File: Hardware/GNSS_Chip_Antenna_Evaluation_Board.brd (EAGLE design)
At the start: 61 x 35.6 mm, 70 parts, among them J1 U.FL, J2 U.FL, J3 U.FL, J4 U.FL, J5 U.FL, J6 U.FL, Y2 PUCK, Y3 CUBE, Y4 CHIP, Y5 MOLDED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

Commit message: Removing lib. Adding test result images.
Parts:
- R1: device Testing:0402-RES -> SparkFun-Resistors:0402
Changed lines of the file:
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@@
 <?xml version="1.0" encoding="utf-8"?>
 <!DOCTYPE eagle SYSTEM "eagle.dtd">
-<eagle version="9.2.2">
+<eagle version="9.3.0">
 <drawing>
 <settings>
@@
 </element>
 <element name="Y4" library="GNSS_Chip_Antenna_Evaluation_Board" package="MOLEX_GNSS_CHIP" value="CHIP" x="52.07" y="1.143" smashed="yes"/>
-<element name="R1" library="Testing" package="0402-RES" value="0" x="56.007" y="1.651" smashed="yes" rot="R180">
+<element name="R1" library="SparkFun-Resistors" package="0402" value="0" x="56.007" y="1.651" smashed="yes" rot="R180">
 <attribute name="NAME" x="56.896" y="0.9525" size="0.4064" layer="25" rot="R180"/>
-<attribute name="VALUE" x="57.0865" y="2.794" size="0.4064" layer="27" rot="R180"/>
+<attribute name="PROD_ID" value="RES-14244" x="56.007" y="1.651" size="1.778" layer="27" rot="R180" display="off"/>
+<attribute name="VALUE" value="0" x="57.0865" y="2.794" size="0.4064" layer="27" rot="R180"/>
 </element>
 <element name="J4" library="SparkFun-Connectors" package="U.FL" value="U.FL" x="57.716" y="3.81" smashed="yes" rot="R270">
@@
 <contactref element="R1" pad="1"/>
 <contactref element="J4" pad="FEED"/>
-<wire x1="56.657" y1="1.651" x2="57.382" y2="1.651" width="0.878840625" layer="1"/>
+<wire x1="56.587" y1="1.651" x2="57.382" y2="1.651" width="0.878840625" layer="1"/>
 <wire x1="57.716" y1="1.985" x2="57.716" y2="2.285" width="0.878840625" layer="1"/>
 <wire x1="57.716" y1="1.985" x2="57.382" y2="1.651" width="0.878840625" layer="1"/>
@@
 <contactref element="Y4" pad="FEED"/>
 <wire x1="54.453" y1="1.693" x2="53.52" y2="1.693" width="0.4826" layer="1"/>
-<wire x1="55.357" y1="1.651" x2="54.483" y2="1.651" width="0.878840625" layer="1"/>
+<wire x1="55.427" y1="1.651" x2="54.483" y2="1.651" width="0.878840625" layer="1"/>
 <wire x1="54.483" y1="1.651" x2="54.483" y2="1.663" width="0.2032" layer="1"/>
 <wire x1="54.483" y1="1.663" x2="54.453" y2="1.693" width="0.2032" layer="1"/>

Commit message: Pass review: Change silk. Add dims. Revise a few FPs.
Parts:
- removed U$40: (no value), buzzard_labels (14):MOLEX_CUBE6
- removed U$41: (no value), buzzard_labels (14):TE_PUCK5
- removed U$45: (no value), buzzard_labels (61):W3062A1
- added U$43: (no value), buzzard_labels (1):ANTENNA10
- added U$50: (no value), buzzard_labels (1):EVALUATION_BOARD15
- added U$52: (no value), buzzard_labels (1):GNSS_CHIP13
- added U$56: (no value), buzzard_labels (1):MOLEX_CUBE6
- added U$57: (no value), buzzard_labels (1):TE_PUCK7
- added U$58: (no value), buzzard_labels (1):W3062A3
- added U$59: (no value), buzzard_labels (1):W30112
- U$13: device buzzard_labels (13):W30111 -> buzzard_labels (1):TE_PUCK7
- U$19: device buzzard_labels (14):MOLEX_CHIP7 -> buzzard_labels (1):MOLEX_CHIP5
- U$20: device buzzard_labels (14):MOLEX_CUBE6 -> buzzard_labels (1):MOLEX_CHIP5
- U$21: device buzzard_labels (60):MOLEX1 -> buzzard_labels (1):MOLEX0
- U$22: device buzzard_labels (14):TE_PUCK5 -> buzzard_labels (1):MOLEX0
- U$29: device buzzard_labels (60):MOLDED2 -> buzzard_labels (1):MOLDED1
- U$30: device buzzard_labels (60):MOLEX1 -> buzzard_labels (1):MOLDED1
- U$31: device buzzard_labels (60):MOLDED2 -> buzzard_labels (1):MOLEX_CUBE6
- U$33: device buzzard_labels (13):W30111 -> buzzard_labels (1):W30112
- U$35: device buzzard_labels (14):W3062A9 -> buzzard_labels (1):W3062A3
- U$37: device buzzard_labels (14):MOLEX_CHIP7 -> SparkFun-Aesthetics:SFE_LOGO_NAME_FLAME_.1
- Y2: device GNSS_Chip_Antenna_Evaluation_Board:TE_PUCK -> SparkFun-GPS:TE_PUCK
- Y3: device GNSS_Chip_Antenna_Evaluation_Board:MOLEX_GNSS_CUBE -> SparkFun-GPS:MOLEX_GNSS_CUBE
- Y4: device GNSS_Chip_Antenna_Evaluation_Board:MOLEX_GNSS_CHIP -> SparkFun-GPS:MOLEX_GNSS_CHIP
- Y5: device GNSS_Chip_Antenna_Evaluation_Board:MLOEX_GNSS_MOLDED -> SparkFun-GPS:MLOEX_GNSS_MOLDED
- Y6: device GNSS_Chip_Antenna_Evaluation_Board:W3062A -> SparkFun-GPS:W3062A
- Y7: device GNSS_Chip_Antenna_Evaluation_Board:W3011 -> SparkFun-GPS:W3011
- moved U$37 48.3 mm to (12.8, 9.65)
- moved U$20 29.7 mm to (60.5, 16.9), flipped to the bottom
- moved U$31 27.5 mm to (43.1, 12.7)
- moved U$22 27.4 mm to (13.1, 31.8), turned to 0 degrees
- moved U$13 23.1 mm to (25.8, 7.24), flipped to the bottom
- moved U$16 17.8 mm to (36.8, 2.54)
- moved U$42 9.72 mm to (24.1, 5.33)
- moved U$30 8.66 mm to (21.5, 29.5), flipped to the bottom
- moved U$35 1.78 mm to (53.8, 35.8)
- moved U$29 0.25 mm to (12.3, 29.5)
- moved U$33 0.18 mm to (44.5, 27.4)
- moved U$21 0.13 mm to (20.7, 31.8)
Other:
- board text added: "Units in inches"

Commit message: Add schematic title. Bump fiducials. Move version #.
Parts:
- moved FRAME1 3.59 mm to (3.81, -12.7)
- moved JP8 0.13 mm to (49.0, 34.8)
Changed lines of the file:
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@@
 <layer number="44" name="Drills" color="7" fill="1" visible="no" active="yes"/>
 <layer number="45" name="Holes" color="7" fill="1" visible="yes" active="yes"/>
-<layer number="46" name="Milling" color="3" fill="1" visible="yes" active="yes"/>
-<layer number="47" name="Measures" color="7" fill="1" visible="yes" active="yes"/>
+<layer number="46" name="Milling" color="3" fill="1" visible="no" active="yes"/>
+<layer number="47" name="Measures" color="7" fill="1" visible="no" active="yes"/>
 <layer number="48" name="Document" color="7" fill="1" visible="no" active="yes"/>
 <layer number="49" name="ReferenceLC" color="13" fill="1" visible="no" active="yes"/>
@@
 <wire x1="0" y1="0" x2="0" y2="35.56" width="0.2032" layer="20"/>
 <text x="0" y="-0.0635" size="0.0254" layer="214" font="vector">D:/SmartProjects/Snc/a4_bn_logo2.bmp</text>
-<text x="20.701" y="0.254" size="1.27" layer="16" font="vector" ratio="20" rot="MR0">V10</text>
+<text x="19.304" y="0.889" size="1.27" layer="16" font="vector" ratio="20" rot="MR0" align="center">V10</text>
 <wire x1="25.4" y1="35.56" x2="25.4" y2="0" width="0.2032" layer="20"/>
 <text x="67.31" y="39.37" size="1.27" layer="51">0.8mm Board Thickness</text>
@@
 <element name="JP5" library="SparkFun" package="STAND-OFF" value="STAND-OFF" x="45.72" y="20.32" smashed="yes" rot="R180"/>
 <element name="JP6" library="SparkFun" package="STAND-OFF" value="STAND-OFF" x="27.94" y="33.02" smashed="yes" rot="R180"/>
-<element name="JP8" library="SparkFun" package="FIDUCIAL-1X2" value="FIDUCIAL1X2" x="49.022" y="34.671" smashed="yes"/>
+<element name="JP8" library="SparkFun" package="FIDUCIAL-1X2" value="FIDUCIAL1X2" x="49.022" y="34.798" smashed="yes"/>
 <element name="JP9" library="SparkFun" package="FIDUCIAL-1X2" value="FIDUCIAL1X2" x="0.762" y="0.762" smashed="yes"/>
 <element name="U$16" library="SparkFun-Aesthetics" package="OSHW-LOGO-S" value="OSHW-LOGOS" x="36.83" y="2.54" smashed="yes" rot="MR0"/>
-<element name="FRAME1" library="SparkFun-Aesthetics" package="CREATIVE_COMMONS" value="FRAME-LETTER" x="1.27" y="-15.24" smashed="yes">
-<attribute name="DESIGNER" value="" x="1.27" y="-15.24" size="1.778" layer="27" font="vector" ratio="15" display="off"/>
-<attribute name="REV" value="" x="1.27" y="-15.24" size="1.778" layer="27" font="vector" ratio="15" display="off"/>
-</element>
 <element name="J1" library="SparkFun-Connectors" package="U.FL" value="U.FL" x="34.29" y="32.004" smashed="yes" rot="R90">
 <attribute name="NAME" x="31.75" y="30.734" size="0.6096" layer="25" font="vector" ratio="20" rot="R90"/>
@@
 <element name="U$35" library="buzzard_labels (1)" package="W3062A3" value="" x="53.848" y="35.814" smashed="yes" rot="MR270"/>
 <element name="U$37" library="SparkFun-Aesthetics" package="SFE_LOGO_NAME_FLAME_.1" value="" x="12.827" y="9.652" smashed="yes" rot="MR0"/>
+<element name="FRAME1" library="SparkFun-Aesthetics" package="CREATIVE_COMMONS" value="FRAME-LETTER" x="3.81" y="-12.7" smashed="yes">
+<attribute name="DESIGNER" value="" x="3.81" y="-12.7" size="1.778" layer="27" font="vector" ratio="15" display="off"/>
+<attribute name="REV" value="" x="3.81" y="-12.7" size="1.778" layer="27" font="vector" ratio="15" display="off"/>
+</element>
 </elements>
 <signals>
@@
 <contactref element="Y7" pad="1"/>
 <wire x1="38.7934" y1="33.815" x2="39.04" y2="33.815" width="0.1524" layer="1"/>
-<wire x1="38.387" y1="33.815" x2="39.04" y2="33.815" width="0.2032" layer="1"/>
 <wire x1="34.29" y1="33.529" x2="34.576" y2="33.815" width="0.878840625" layer="1"/>
-<wire x1="34.576" y1="33.815" x2="38.387" y2="33.815" width="0.878840625" layer="1"/>
+<wire x1="38.387" y1="33.815" x2="34.576" y2="33.815" width="0.878840625" layer="1"/>
+<wire x1="39.04" y1="33.815" x2="38.387" y2="33.815" width="0.1524" layer="1"/>
 </signal>
 <signal name="FEED3">
@@
 <contactref element="J3" pad="FEED"/>
 <contactref element="Y3" pad="FEED"/>
-<wire x1="31.36158125" y1="9.779" x2="31.39058125" y2="9.75" width="0.878840625" layer="1"/>
 <wire x1="29.465" y1="9.779" x2="31.36158125" y2="9.779" width="0.878840625" layer="1"/>
 <wire x1="31.5" y1="9.75" x2="31.471" y2="9.779" width="0.2032" layer="1"/>
@@
 <contactref element="J5" pad="FEED"/>
 <wire x1="2.159" y1="29.211003125" x2="2.159" y2="32.004996875" width="0.878840625" layer="1"/>
-<wire x1="2.159" y1="32.004996875" x2="2.114" y2="32.049996875" width="0.878840625" layer="1"/>
 <wire x1="2.114" y1="32.05" x2="2.159" y2="32.005" width="0.2032" layer="1"/>
 <wire x1="2.159" y1="32.005" x2="2.159" y2="32.004996875" width="0.2032" layer="1"/>

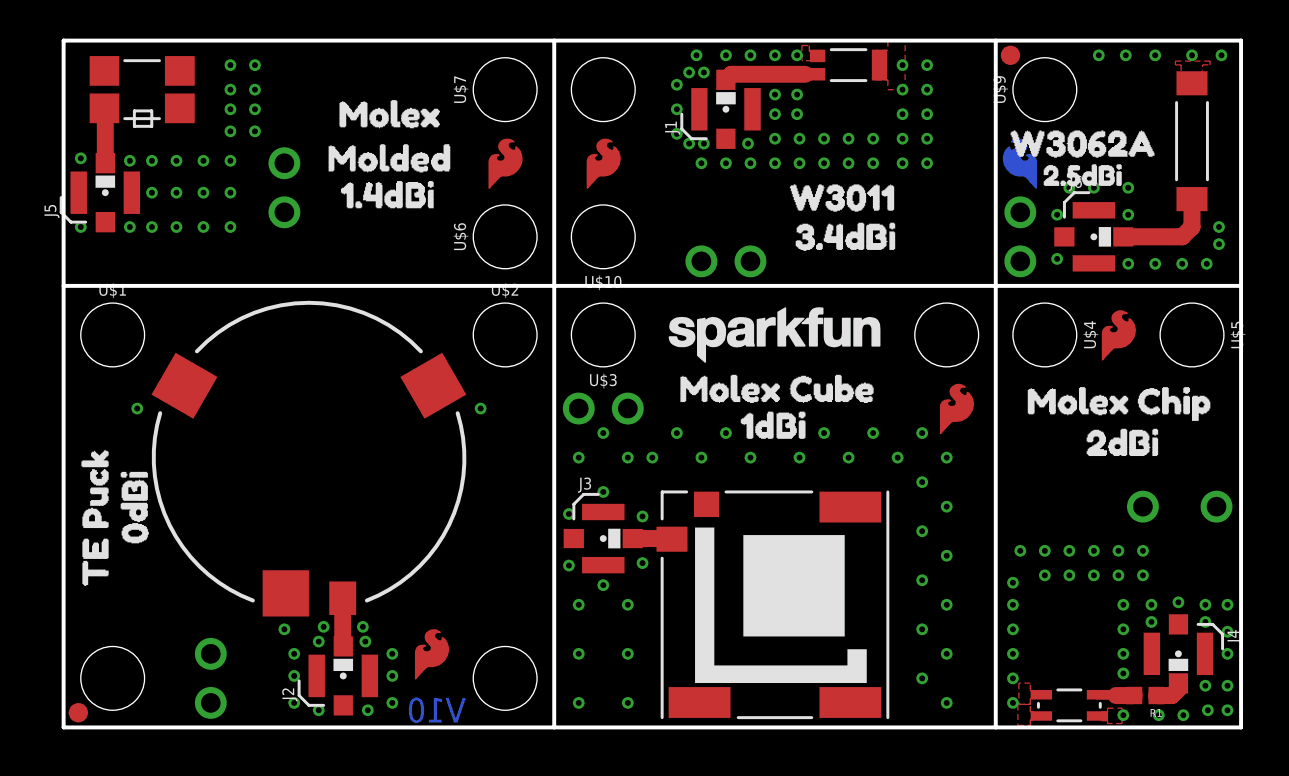
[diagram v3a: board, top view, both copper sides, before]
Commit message: Corrected the polygon FP issue on the U.FL.
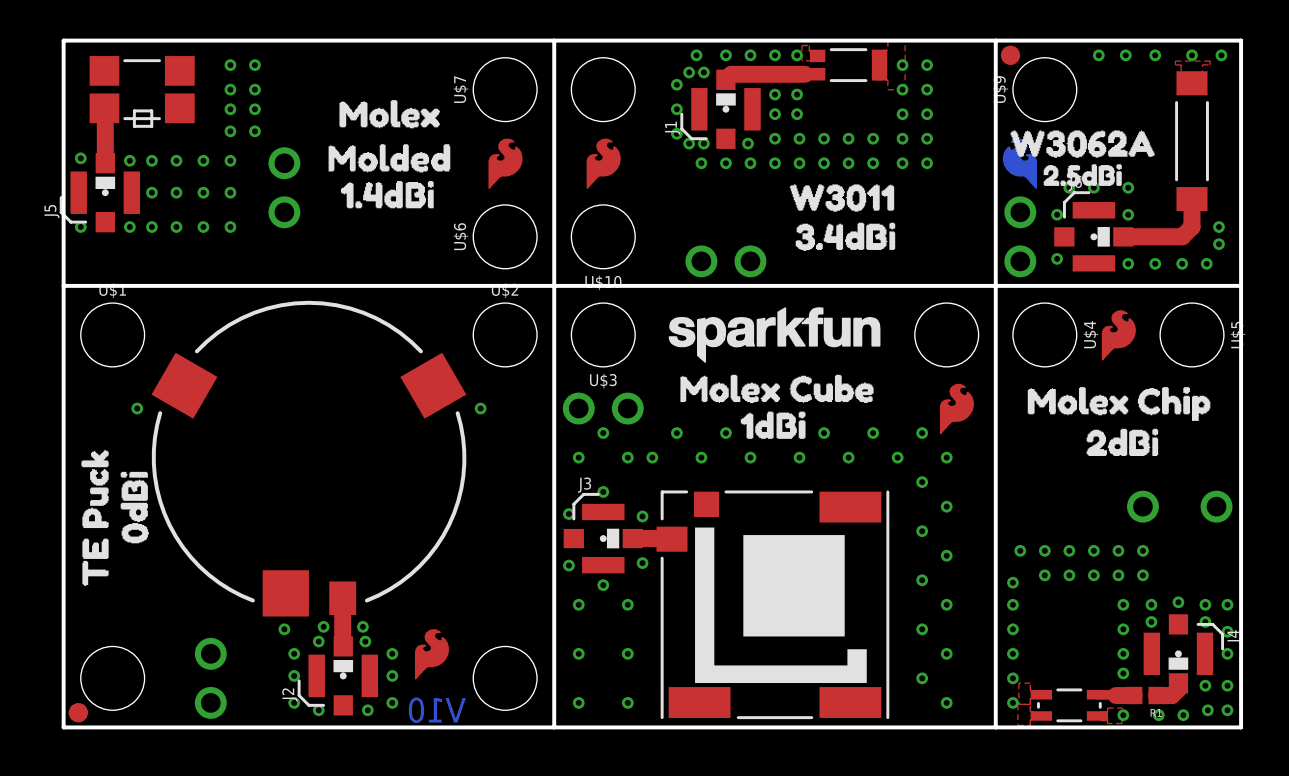
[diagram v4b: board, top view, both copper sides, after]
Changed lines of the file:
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@@
 <layer number="23" name="tOrigins" color="15" fill="1" visible="yes" active="yes"/>
 <layer number="24" name="bOrigins" color="15" fill="1" visible="yes" active="yes"/>
-<layer number="25" name="tNames" color="7" fill="1" visible="no" active="yes"/>
-<layer number="26" name="bNames" color="7" fill="1" visible="no" active="yes"/>
-<layer number="27" name="tValues" color="7" fill="1" visible="no" active="yes"/>
-<layer number="28" name="bValues" color="7" fill="1" visible="no" active="yes"/>
-<layer number="29" name="tStop" color="2" fill="3" visible="no" active="yes"/>
-<layer number="30" name="bStop" color="5" fill="6" visible="no" active="yes"/>
-<layer number="31" name="tCream" color="7" fill="4" visible="no" active="yes"/>
-<layer number="32" name="bCream" color="7" fill="5" visible="no" active="yes"/>
-<layer number="33" name="tFinish" color="6" fill="3" visible="no" active="yes"/>
-<layer number="34" name="bFinish" color="6" fill="6" visible="no" active="yes"/>
-<layer number="35" name="tGlue" color="7" fill="4" visible="no" active="yes"/>
-<layer number="36" name="bGlue" color="7" fill="5" visible="no" active="yes"/>
-<layer number="37" name="tTest" color="7" fill="1" visible="no" active="yes"/>
-<layer number="38" name="bTest" color="7" fill="1" visible="no" active="yes"/>
-<layer number="39" name="tKeepout" color="4" fill="11" visible="no" active="yes"/>
-<layer number="40" name="bKeepout" color="1" fill="11" visible="no" active="yes"/>
-<layer number="41" name="tRestrict" color="4" fill="10" visible="no" active="yes"/>
-<layer number="42" name="bRestrict" color="1" fill="10" visible="no" active="yes"/>
-<layer number="43" name="vRestrict" color="2" fill="10" visible="no" active="yes"/>
-<layer number="44" name="Drills" color="7" fill="1" visible="no" active="yes"/>
+<layer number="25" name="tNames" color="7" fill="1" visible="yes" active="yes"/>
+<layer number="26" name="bNames" color="7" fill="1" visible="yes" active="yes"/>
+<layer number="27" name="tValues" color="7" fill="1" visible="yes" active="yes"/>
+<layer number="28" name="bValues" color="7" fill="1" visible="yes" active="yes"/>
+<layer number="29" name="tStop" color="2" fill="3" visible="yes" active="yes"/>
+<layer number="30" name="bStop" color="5" fill="6" visible="yes" active="yes"/>
+<layer number="31" name="tCream" color="7" fill="4" visible="yes" active="yes"/>
+<layer number="32" name="bCream" color="7" fill="5" visible="yes" active="yes"/>
+<layer number="33" name="tFinish" color="6" fill="3" visible="yes" active="yes"/>
+<layer number="34" name="bFinish" color="6" fill="6" visible="yes" active="yes"/>
+<layer number="35" name="tGlue" color="7" fill="4" visible="yes" active="yes"/>
+<layer number="36" name="bGlue" color="7" fill="5" visible="yes" active="yes"/>
+<layer number="37" name="tTest" color="7" fill="1" visible="yes" active="yes"/>
+<layer number="38" name="bTest" color="7" fill="1" visible="yes" active="yes"/>
+<layer number="39" name="tKeepout" color="4" fill="11" visible="yes" active="yes"/>
+<layer number="40" name="bKeepout" color="1" fill="11" visible="yes" active="yes"/>
+<layer number="41" name="tRestrict" color="4" fill="10" visible="yes" active="yes"/>
+<layer number="42" name="bRestrict" color="1" fill="10" visible="yes" active="yes"/>
+<layer number="43" name="vRestrict" color="2" fill="10" visible="yes" active="yes"/>
+<layer number="44" name="Drills" color="7" fill="1" visible="yes" active="yes"/>
 <layer number="45" name="Holes" color="7" fill="1" visible="yes" active="yes"/>
-<layer number="46" name="Milling" color="3" fill="1" visible="no" active="yes"/>
-<layer number="47" name="Measures" color="7" fill="1" visible="no" active="yes"/>
-<layer number="48" name="Document" color="7" fill="1" visible="no" active="yes"/>
-<layer number="49" name="ReferenceLC" color="13" fill="1" visible="no" active="yes"/>
-<layer number="50" name="ReferenceLS" color="12" fill="1" visible="no" active="yes"/>
+<layer number="46" name="Milling" color="3" fill="1" visible="yes" active="yes"/>
+<layer number="47" name="Measures" color="7" fill="1" visible="yes" active="yes"/>
+<layer number="48" name="Document" color="7" fill="1" visible="yes" active="yes"/>
+<layer number="49" name="ReferenceLC" color="13" fill="1" visible="yes" active="yes"/>
+<layer number="50" name="ReferenceLS" color="12" fill="1" visible="yes" active="yes"/>
 <layer number="51" name="tDocu" color="6" fill="1" visible="yes" active="yes"/>
-<layer number="52" name="bDocu" color="7" fill="1" visible="no" active="yes"/>
+<layer number="52" name="bDocu" color="7" fill="1" visible="yes" active="yes"/>
 <layer number="91" name="Nets" color="2" fill="1" visible="no" active="no"/>
 <layer number="92" name="Busses" color="1" fill="1" visible="no" active="no"/>
